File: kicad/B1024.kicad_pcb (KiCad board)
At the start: 2 copper layers, 234 x 147.2 mm, 121 parts, among them J1 "RESET", J2 "0FFF/0800 EN", J3 "LED", J4 "RAM ROM", J5 EXP, J6 EXP, J9 COPRO, P7 EXP, P9 COPRO, U1 6264, U10 74153, U11 74153, U12 41256, U13 41256, U14 41256, U15 41256, U16 41256, U17 41256, U18 41256, U19 41256, U2 74LS85, U20 41256, U21 41256, U22 41256, U23 41256, U24 41256, U25 41256, U26 41256, U27 41256, U28 41256, U29 41256, U3 74LS74, U30 41256, U31 41256, U32 41256, U33 41256, U34 41256, U35 41256, U36 41256, U37 41256, U38 41256, U39 41256, U4 74LS08, U40 41256, U41 41256, U42 41256, U43 41256, U44 74LS157, U45 74LS139, U46 74LS157, U47 74LS153, U5 74LS02, U6 74LS393, U7 74153, U8 74153, U9 74153

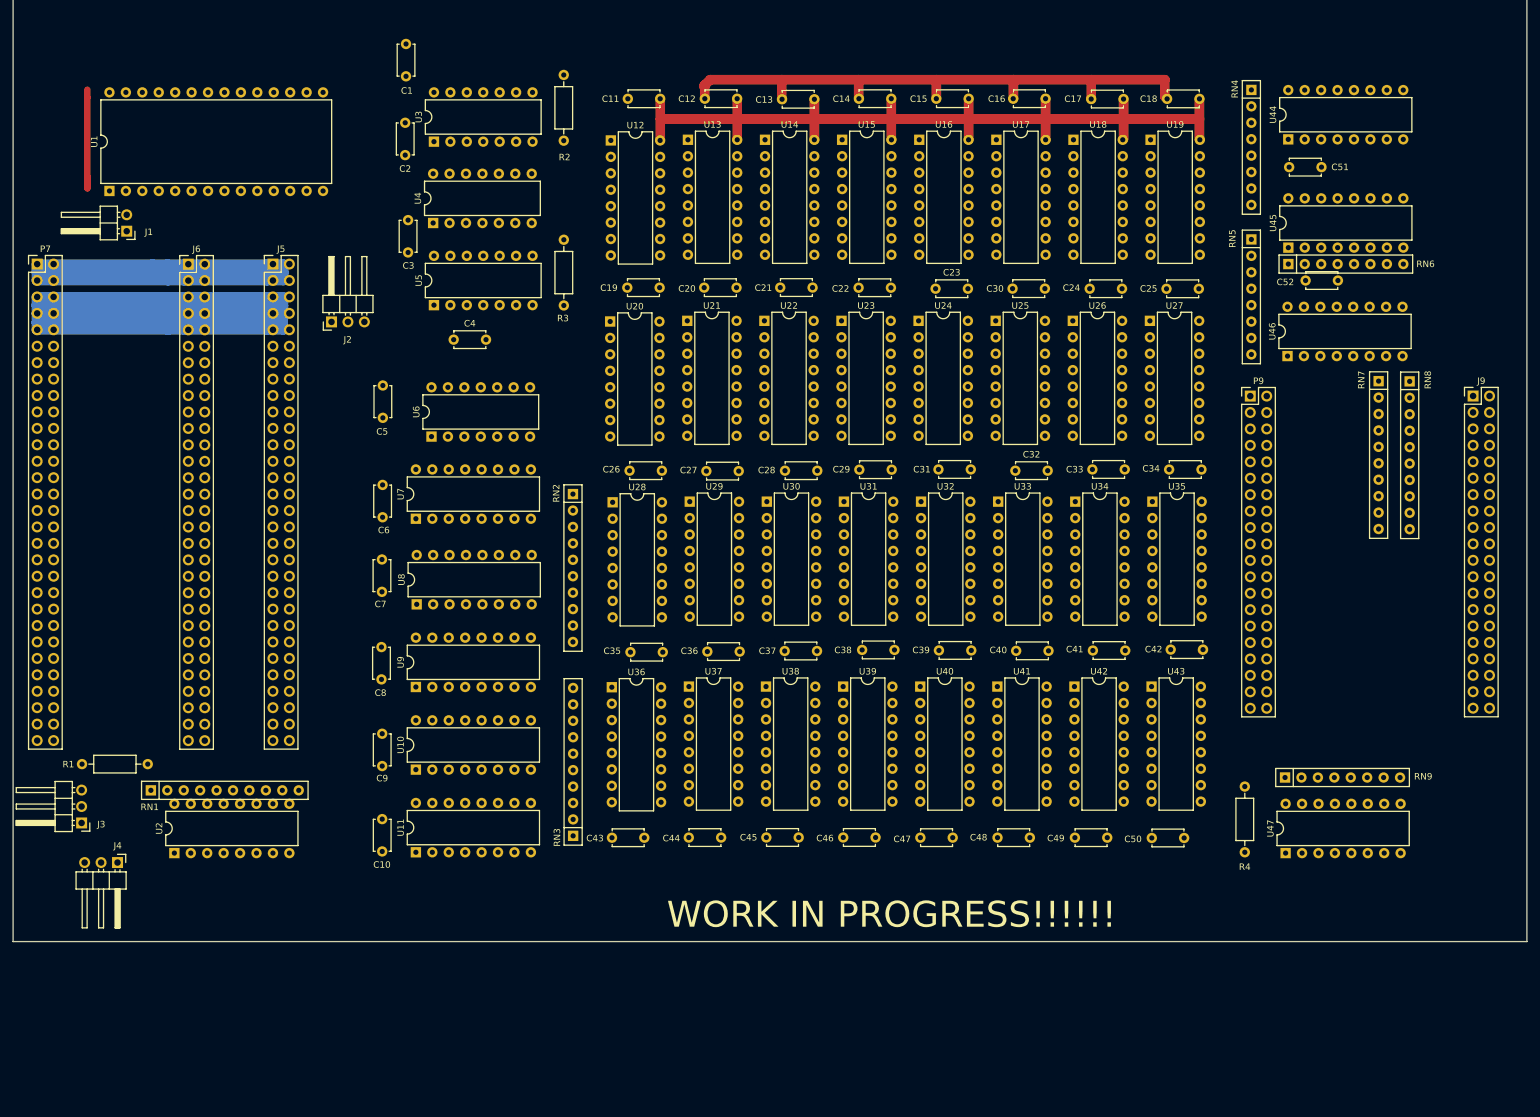
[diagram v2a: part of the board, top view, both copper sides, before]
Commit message: Routing and circuit updates
Schematic is starting to take shape. Route most common dram line and
many expansion lines.
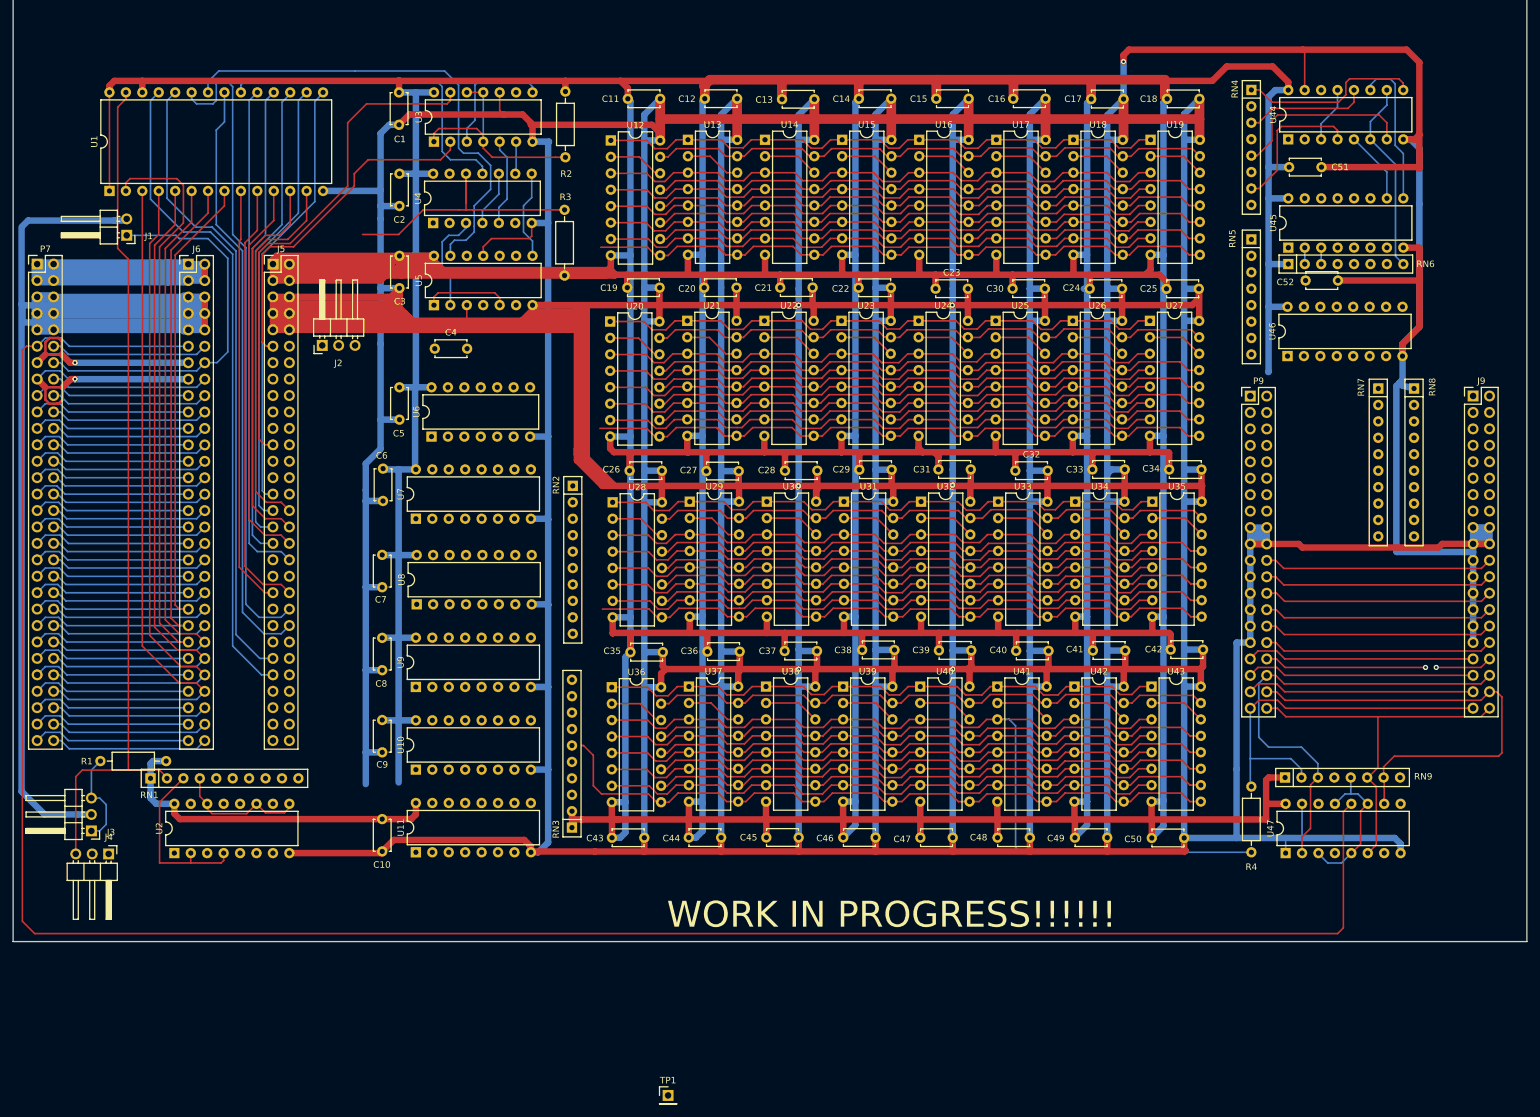
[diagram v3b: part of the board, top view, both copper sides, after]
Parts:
- added TP1: TestPoint, Connector_PinHeader_2.54mm:PinHeader_1x01_P2.54mm_Vertical, F.Cu at (138.4, 184.7)
- moved R3 14.8 mm to (122.4, 47.8), turned to 270 degrees
- moved C2 7.92 mm to (96.9, 42.2)
- moved C1 7.57 mm to (96.8, 29.6)
- moved C6 7.52 mm to (94.4, 87.8), turned to 270 degrees
- moved C3 5.68 mm to (96.9, 54.9)
- moved J2 3.91 mm to (85.0, 68.7)
- moved C4 3.24 mm to (102.4, 69.2)
- moved R1 2.88 mm to (50.7, 133.0)
- moved C5 2.58 mm to (96.9, 75.2)
- moved R2 2.58 mm to (122.6, 39.6)
- moved C9 2.12 mm to (94.2, 126.6)
- moved J3 1.95 mm to (49.3, 143.8)
- moved J4 1.91 mm to (51.9, 147.3)
- moved RN1 1.85 mm to (58.4, 135.6)
- moved C8 1.43 mm to (94.2, 113.9)
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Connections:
- C4 pad 1: 5V -> (no net)
- C4 pad 2: GND -> (no net)
- J1 pad 1: (no net) -> ~EXTRES
- J1 pad 2: (no net) -> GND
- J3 pad 1: (no net) -> Net-(J3-Pad1)
- J3 pad 2: (no net) -> GND
- J3 pad 3: (no net) -> Net-(J3-Pad1)
- J4 pad 1: Net-(J4-Pad1) -> (no net)
- J4 pad 3: (no net) -> Net-(J4-Pad3)
- R1 pad 1: (no net) -> Net-(J3-Pad1)
- R1 pad 2: (no net) -> 5V
- R2 pad 1: (no net) -> Net-(R2-Pad1)
- R2 pad 2: (no net) -> 5V
- R3 pad 1: (no net) -> Net-(R3-Pad1)
- R3 pad 2: (no net) -> 5V
- R4 pad 1: (no net) -> ~W
- R4 pad 2: (no net) -> DRAM-RW
- RN1 pad 1: (no net) -> 5V
- RN1 pad 2: (no net) -> Net-(J4-Pad3)
- RN1 pad 3: (no net) -> Net-(RN1-Pad3)
- RN1 pad 4: (no net) -> Net-(RN1-Pad4)
- RN3 pad 1: (no net) -> 5V
- RN3 pad 2: (no net) -> 5V
- RN4 pad 1: (no net) -> Net-(RN4-Pad1)
- RN4 pad 3: (no net) -> Net-(RN4-Pad3)
- RN4 pad 5: (no net) -> Net-(RN4-Pad5)
- RN4 pad 7: (no net) -> Net-(RN4-Pad7)
- RN6 pad 1: (no net) -> 5V
- RN6 pad 2: (no net) -> Net-(RN6-Pad2)
- RN6 pad 3: (no net) -> Net-(RN6-Pad3)
- RN6 pad 8: (no net) -> Net-(RN6-Pad8)
- RN8 pad 1: (no net) -> GND
- RN9 pad 2: (no net) -> DRAM-RW
- RN9 pad 3: (no net) -> ~BUSY
- RN9 pad 5: (no net) -> Net-(RN9-Pad5)
- RN9 pad 6: (no net) -> ~ECAS
- RN9 pad 7: (no net) -> ~ERAS
- U1 pad 20: (no net) -> Net-(U1-Pad20)
- U1 pad 22: (no net) -> Net-(U1-Pad22)
- U1 pad 26: (no net) -> 5V
- U1 pad 27: Net-(J4-Pad1) -> Net-(J4-Pad3)
- U12 pad 14: D -> Net-(U12-Pad14)
- U12 pad 2: D -> Net-(U12-Pad14)
- U13 pad 14: D -> Net-(U13-Pad14)
- U13 pad 2: D -> Net-(U13-Pad14)
- U14 pad 14: D -> Net-(U14-Pad14)
- U14 pad 2: D -> Net-(U14-Pad14)
- U15 pad 14: D -> Net-(U15-Pad14)
- U15 pad 2: D -> Net-(U15-Pad14)
- U16 pad 14: D -> Net-(U16-Pad14)
- U16 pad 2: D -> Net-(U16-Pad14)
- U17 pad 14: D -> Net-(U17-Pad14)
- U17 pad 2: D -> Net-(U17-Pad14)
- U18 pad 14: D -> Net-(U18-Pad14)
- U18 pad 2: D -> Net-(U18-Pad14)
- U19 pad 14: D -> Net-(U19-Pad14)
- U19 pad 2: D -> Net-(U19-Pad14)
- U2 pad 11: (no net) -> Net-(RN1-Pad4)
- U2 pad 14: (no net) -> Net-(RN1-Pad4)
- U2 pad 2: (no net) -> Net-(RN1-Pad3)
- U2 pad 4: (no net) -> Net-(RN1-Pad3)
- U2 pad 9: (no net) -> Net-(RN1-Pad4)
- U20 pad 14: D -> Net-(U20-Pad14)
- U20 pad 2: D -> Net-(U20-Pad14)
- U21 pad 14: D -> Net-(U21-Pad14)
- U21 pad 2: D -> Net-(U21-Pad14)
- U22 pad 14: D -> Net-(U22-Pad14)
- U22 pad 2: D -> Net-(U22-Pad14)
- U23 pad 14: D -> Net-(U23-Pad14)
- U23 pad 2: D -> Net-(U23-Pad14)
- U24 pad 14: D -> Net-(U24-Pad14)
- U24 pad 2: D -> Net-(U24-Pad14)
- U25 pad 14: D -> Net-(U25-Pad14)
- U25 pad 2: D -> Net-(U25-Pad14)
- U26 pad 14: D -> Net-(U26-Pad14)
- U26 pad 2: D -> Net-(U26-Pad14)
- U27 pad 14: D -> Net-(U27-Pad14)
- U27 pad 2: D -> Net-(U27-Pad14)
- U28 pad 14: D -> Net-(U28-Pad14)
- U28 pad 2: D -> Net-(U28-Pad14)
- U29 pad 14: D -> Net-(U29-Pad14)
- U29 pad 2: D -> Net-(U29-Pad14)
- U3 pad 1: (no net) -> Net-(R2-Pad1)
- U3 pad 10: (no net) -> GND
- U3 pad 11: (no net) -> Net-(R2-Pad1)
- U3 pad 12: (no net) -> Net-(R2-Pad1)
- U3 pad 13: (no net) -> BOOTCLK
- U3 pad 2: (no net) -> ~BRAS
- U3 pad 3: (no net) -> Net-(U3-Pad3)
- U3 pad 4: (no net) -> Net-(R2-Pad1)
- U3 pad 5: (no net) -> Net-(U3-Pad5)
- U3 pad 6: (no net) -> Net-(U3-Pad6)
- U3 pad 8: (no net) -> Net-(U3-Pad3)
- U30 pad 14: D -> Net-(U30-Pad14)
- U30 pad 2: D -> Net-(U30-Pad14)
- U31 pad 14: D -> Net-(U31-Pad14)
- U31 pad 2: D -> Net-(U31-Pad14)
- U32 pad 14: D -> Net-(U32-Pad14)
- U32 pad 2: D -> Net-(U32-Pad14)
- U33 pad 14: D -> Net-(U33-Pad14)
- U33 pad 2: D -> Net-(U33-Pad14)
- U34 pad 14: D -> Net-(U34-Pad14)
- U34 pad 2: D -> Net-(U34-Pad14)
- U35 pad 14: D -> Net-(U35-Pad14)
- U35 pad 2: D -> Net-(U35-Pad14)
- U36 pad 14: D -> Net-(U36-Pad14)
- U36 pad 2: D -> Net-(U36-Pad14)
- U37 pad 14: D -> Net-(U37-Pad14)
- U37 pad 2: D -> Net-(U37-Pad14)
- U38 pad 14: D -> Net-(U38-Pad14)
- U38 pad 2: D -> Net-(U38-Pad14)
- U39 pad 14: D -> Net-(U39-Pad14)
- U39 pad 2: D -> Net-(U39-Pad14)
- U4 pad 10: (no net) -> Net-(U4-Pad10)
- U4 pad 11: (no net) -> Net-(U1-Pad20)
- U4 pad 12: (no net) -> Net-(R3-Pad1)
- U4 pad 3: (no net) -> Net-(U4-Pad3)
- U4 pad 4: (no net) -> Net-(U4-Pad10)
- U4 pad 5: (no net) -> Net-(U3-Pad5)
- U4 pad 8: (no net) -> Net-(U4-Pad8)
- U4 pad 9: (no net) -> Net-(U3-Pad6)
- U40 pad 14: D -> Net-(U40-Pad14)
- U40 pad 2: D -> Net-(U40-Pad14)
- U41 pad 14: D -> Net-(U41-Pad14)
- U41 pad 2: D -> Net-(U41-Pad14)
- U42 pad 14: D -> Net-(U42-Pad14)
- U42 pad 2: D -> Net-(U42-Pad14)
- U43 pad 14: D -> Net-(U43-Pad14)
- U43 pad 2: D -> Net-(U43-Pad14)
- U44 pad 10: (no net) -> Net-(RN6-Pad8)
- U44 pad 11: (no net) -> Net-(U44-Pad11)
- U44 pad 12: (no net) -> Net-(RN4-Pad3)
- U44 pad 13: (no net) -> Net-(U44-Pad13)
- U44 pad 15: (no net) -> GND
- U44 pad 3: (no net) -> Net-(U44-Pad13)
- U44 pad 4: (no net) -> Net-(RN4-Pad7)
- U44 pad 5: (no net) -> Net-(U44-Pad5)
- U44 pad 6: (no net) -> Net-(RN6-Pad8)
- U44 pad 7: (no net) -> Net-(RN4-Pad5)
- U44 pad 9: (no net) -> Net-(RN4-Pad1)
- U45 pad 10: (no net) -> Net-(U44-Pad5)
- U45 pad 16: GND -> 5V
- U45 pad 2: (no net) -> Net-(RN6-Pad2)
- U45 pad 3: (no net) -> Net-(RN6-Pad3)
- U45 pad 8: 5V -> GND
- U45 pad 9: (no net) -> Net-(U44-Pad11)
- U46 pad 10: (no net) -> Net-(U46-Pad10)
- U46 pad 13: (no net) -> Net-(U46-Pad13)
- U46 pad 3: (no net) -> Net-(U46-Pad13)
- U46 pad 6: (no net) -> Net-(U46-Pad10)
- U47 pad 1: (no net) -> GND
- U47 pad 10: (no net) -> ~ERAS
- U47 pad 11: (no net) -> Net-(RN9-Pad5)
- U47 pad 12: (no net) -> ~BRAS
- U47 pad 13: (no net) -> Net-(RN9-Pad5)
- U47 pad 15: (no net) -> GND
- U47 pad 2: (no net) -> ~BUSY
- U47 pad 3: (no net) -> Net-(RN9-Pad5)
- U47 pad 5: (no net) -> Net-(RN9-Pad5)
- U47 pad 6: (no net) -> ~ECAS
- U5 pad 1: (no net) -> Net-(U5-Pad1)
- U5 pad 11: (no net) -> GND
- U5 pad 13: (no net) -> Net-(U1-Pad22)
- U5 pad 2: (no net) -> Net-(U4-Pad3)
- U5 pad 3: (no net) -> GND
- U5 pad 5: (no net) -> Net-(U5-Pad1)
- U5 pad 8: (no net) -> Net-(U4-Pad8)
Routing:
- net GND: track 452.4 -> 3348.9 mm, vias 0 -> 7
- net 5V: track 252.4 -> 2079.8 mm
- net ~W: track 0.00 -> 422.7 mm
- net DRAMA7: track 0.00 -> 414.9 mm
- net ~BRAS: track 0.00 -> 394.0 mm
- net DRAMA5: track 0.00 -> 364.3 mm
- net DRAMA1: track 0.00 -> 363.8 mm
- net ~RAS: track 0.00 -> 363.8 mm
- net DRAMA3: track 0.00 -> 363.8 mm
- net DRAMA6: track 0.00 -> 363.8 mm
- net DRAMA4: track 0.00 -> 363.8 mm
- net DRAMA8: track 0.00 -> 363.6 mm
- net DRAMA2: track 0.00 -> 363.4 mm
- net DRAMA0: track 0.00 -> 363.4 mm
- net ~CAS: track 0.00 -> 361.9 mm
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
